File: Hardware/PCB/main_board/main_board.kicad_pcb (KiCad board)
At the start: 2 copper layers, 150 x 160 mm, 125 parts, among them J1 SWD, J2 USB_A, J3 DIN-5_180degree, J4 USB_B, J5 Conn_Coaxial, J6 AudioJack3, Q1 BC857B, Q2 BC847B, Q3 BC847B, Q4 BC857B, Q5 BC847B, U1 MCP6002-xSN, U2 NUCLEO-F446RE, U3 6N137, U4 RC4558, U5 MCP6002-xSN

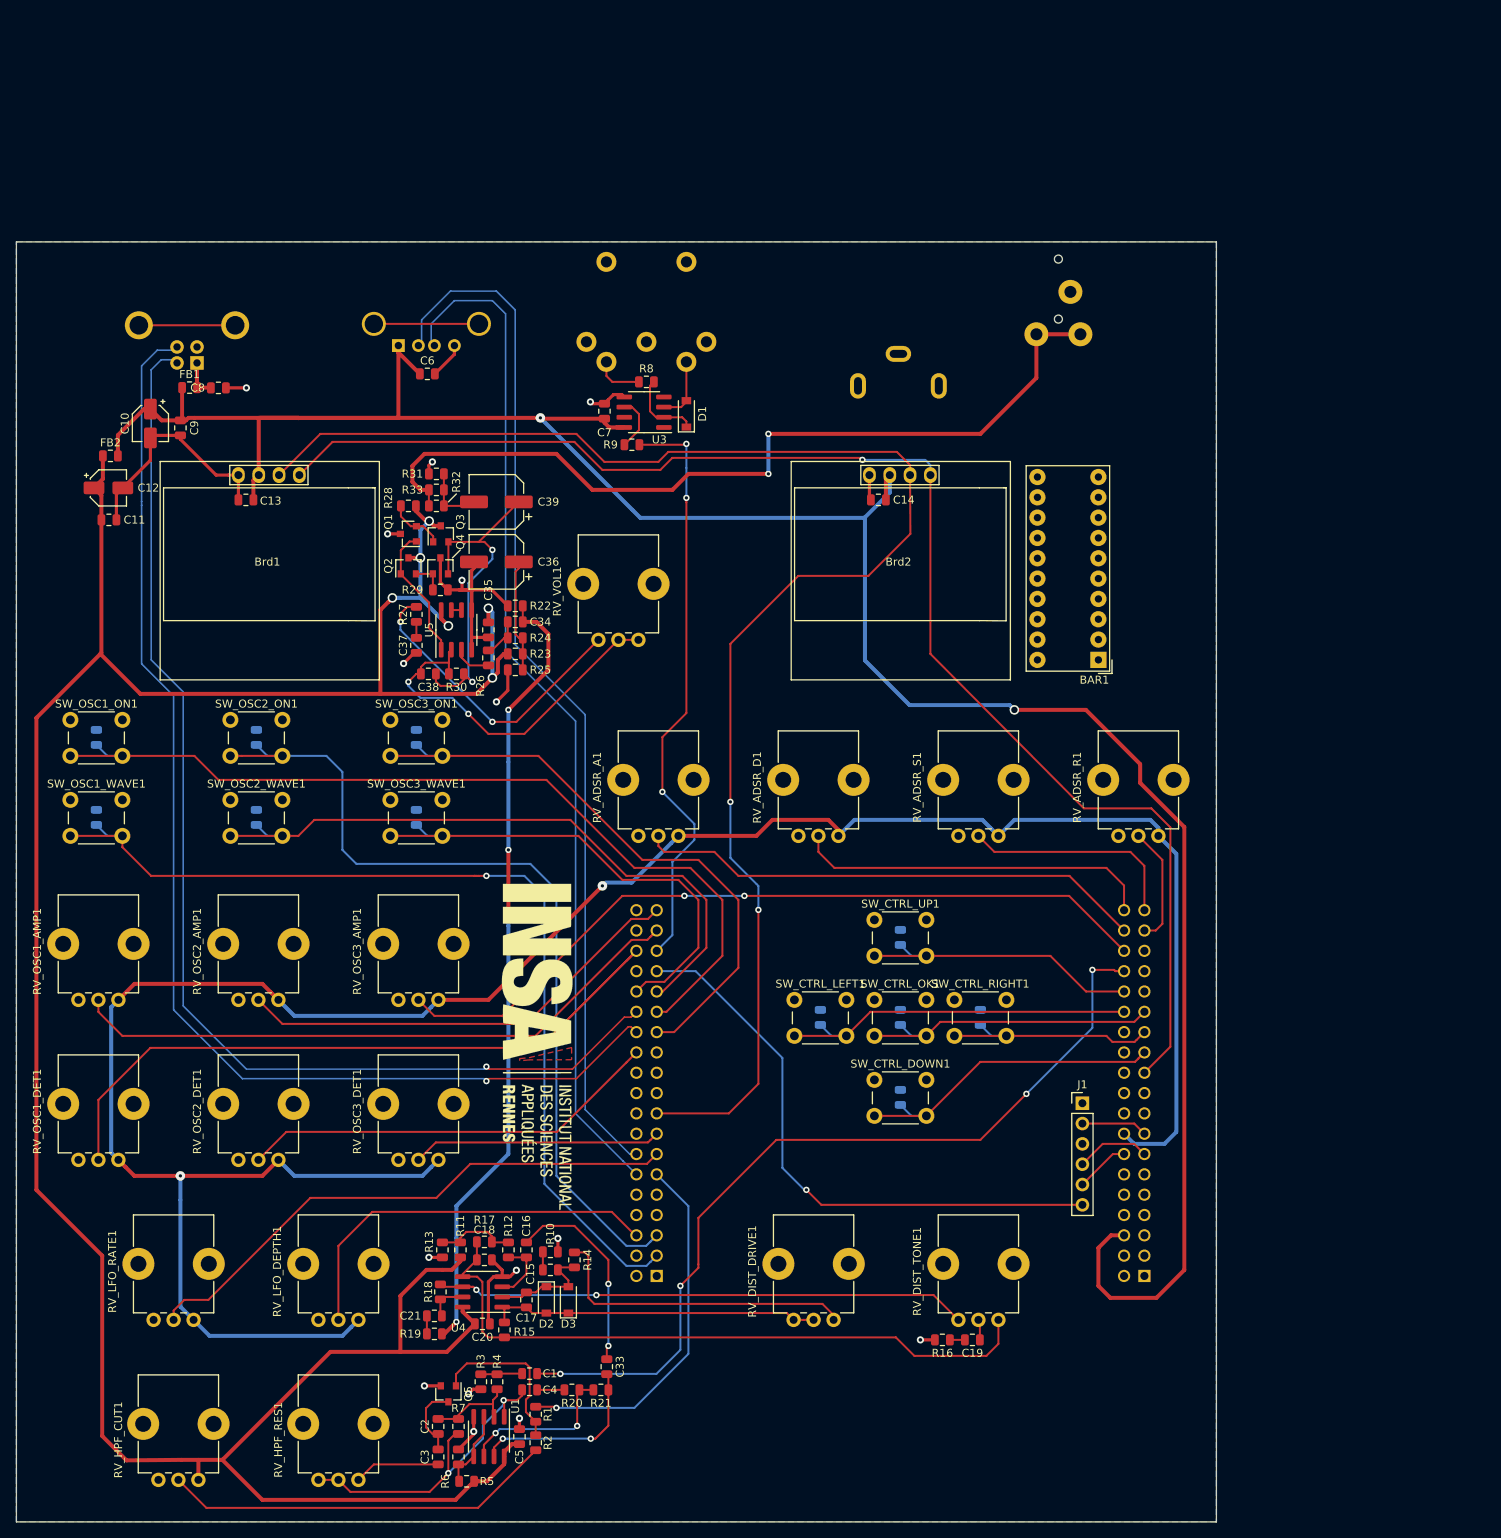
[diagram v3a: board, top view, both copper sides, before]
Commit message: Add test points headers
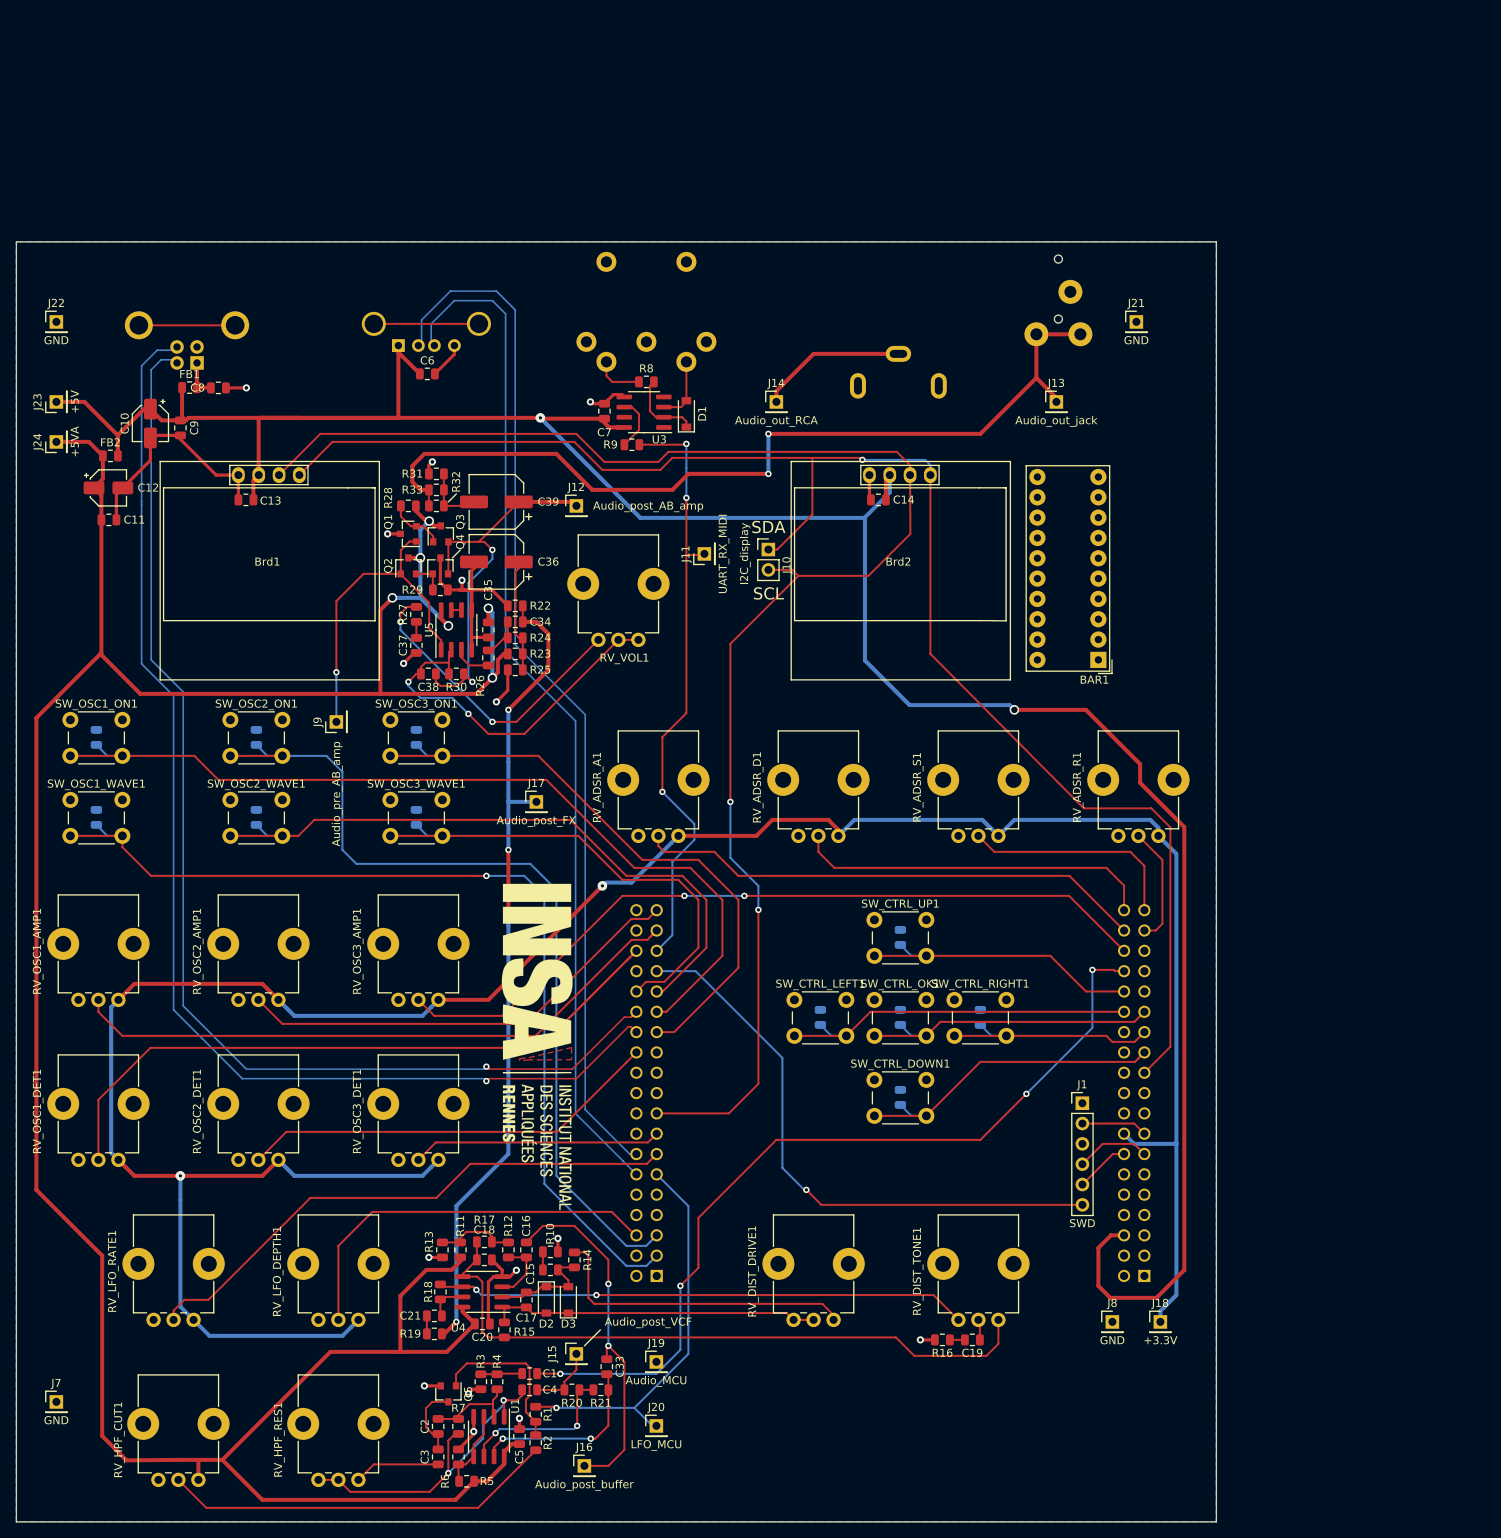
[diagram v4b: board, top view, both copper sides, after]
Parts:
- added J10: I2C_display, Connector_PinHeader_2.54mm:PinHeader_1x02_P2.54mm_Vertical, F.Cu at (129.0, 98.5)
- added J11: UART_RX_MIDI, Connector_PinHeader_2.54mm:PinHeader_1x01_P2.54mm_Vertical, F.Cu at (121.0, 99.0)
- added J12: Audio_post_AB_amp, Connector_PinHeader_2.54mm:PinHeader_1x01_P2.54mm_Vertical, F.Cu at (105.0, 93.0)
- added J13: Audio_out_jack, Connector_PinHeader_2.54mm:PinHeader_1x01_P2.54mm_Vertical, F.Cu at (165.0, 80.0)
- added J14: Audio_out_RCA, Connector_PinHeader_2.54mm:PinHeader_1x01_P2.54mm_Vertical, F.Cu at (130.0, 80.0)
- added J15: Audio_post_VCF, Connector_PinHeader_2.54mm:PinHeader_1x01_P2.54mm_Vertical, F.Cu at (105.0, 199.0)
- added J16: Audio_post_buffer, Connector_PinHeader_2.54mm:PinHeader_1x01_P2.54mm_Vertical, F.Cu at (106.0, 213.0)
- added J17: Audio_post_FX, Connector_PinHeader_2.54mm:PinHeader_1x01_P2.54mm_Vertical, F.Cu at (100.0, 130.0)
- added J18: +3.3V, Connector_PinHeader_2.54mm:PinHeader_1x01_P2.54mm_Vertical, F.Cu at (178.0, 195.0)
- added J19: Audio_MCU, Connector_PinHeader_2.54mm:PinHeader_1x01_P2.54mm_Vertical, F.Cu at (115.0, 200.0)
- added J20: LFO_MCU, Connector_PinHeader_2.54mm:PinHeader_1x01_P2.54mm_Vertical, F.Cu at (115.0, 208.0)
- added J21: GND, Connector_PinHeader_2.54mm:PinHeader_1x01_P2.54mm_Vertical, F.Cu at (175.0, 70.0)
- added J22: GND, Connector_PinHeader_2.54mm:PinHeader_1x01_P2.54mm_Vertical, F.Cu at (40.0, 70.0)
- added J23: +5V, Connector_PinHeader_2.54mm:PinHeader_1x01_P2.54mm_Vertical, F.Cu at (40.0, 80.0)
- added J24: +5VA, Connector_PinHeader_2.54mm:PinHeader_1x01_P2.54mm_Vertical, F.Cu at (40.0, 85.0)
- added J7: GND, Connector_PinHeader_2.54mm:PinHeader_1x01_P2.54mm_Vertical, F.Cu at (40.0, 205.0)
- added J8: GND, Connector_PinHeader_2.54mm:PinHeader_1x01_P2.54mm_Vertical, F.Cu at (172.0, 195.0)
- added J9: Audio_pre_AB_amp, Connector_PinHeader_2.54mm:PinHeader_1x01_P2.54mm_Vertical, F.Cu at (75.0, 120.0)
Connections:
- net Net-(C38-Pad1) renamed /audio_out/audio_post_AB_amp
- net Net-(J6-PadR) renamed /audio_out/Audio_out_jack
- net Net-(Q1-Pad1) renamed /audio_out/audio_pre_AB_amp
- J5 pad 1: Net-(J5-Pad1) -> /audio_out/Audio_out_RCA
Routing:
- net /audio_out/audio_pre_AB_amp: track 16.9 -> 41.5 mm, vias 0 -> 1
- net +3V3: track 298.4 -> 322.5 mm
- net /analogFX/IN_DIST: track 25.4 -> 45.0 mm
- net /audio_out/Audio_out_RCA: track 0.00 -> 18.5 mm
- net /HMI/I2C_display_SDA: track 177.7 -> 192.1 mm
- net +5V: track 319.7 -> 329.1 mm
- net /audio_out/audio_post_AB_amp: track 42.1 -> 49.5 mm
- net +5VA: track 356.7 -> 363.2 mm
- net /analogFX/OUT_VCF: track 3.41 -> 8.53 mm
- net /HMI/I2C_display_SCL: track 191.1 -> 195.2 mm
- net /audio_out/Audio_out_jack: track 106.6 -> 110.7 mm
- net /analogFX/CV_IN: track 46.0 -> 49.7 mm
- net /audio_out/AUDIO_IN: track 99.0 -> 102.5 mm
- net /MIDI/MIDI_Serial_RX: track 74.1 -> 76.5 mm
- net /analogFX/AUDIO_IN: track 107.0 -> 108.1 mm
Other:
- board text added: "SCL"
- board text added: "SDA"

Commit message: Re-layout HMI, pre route
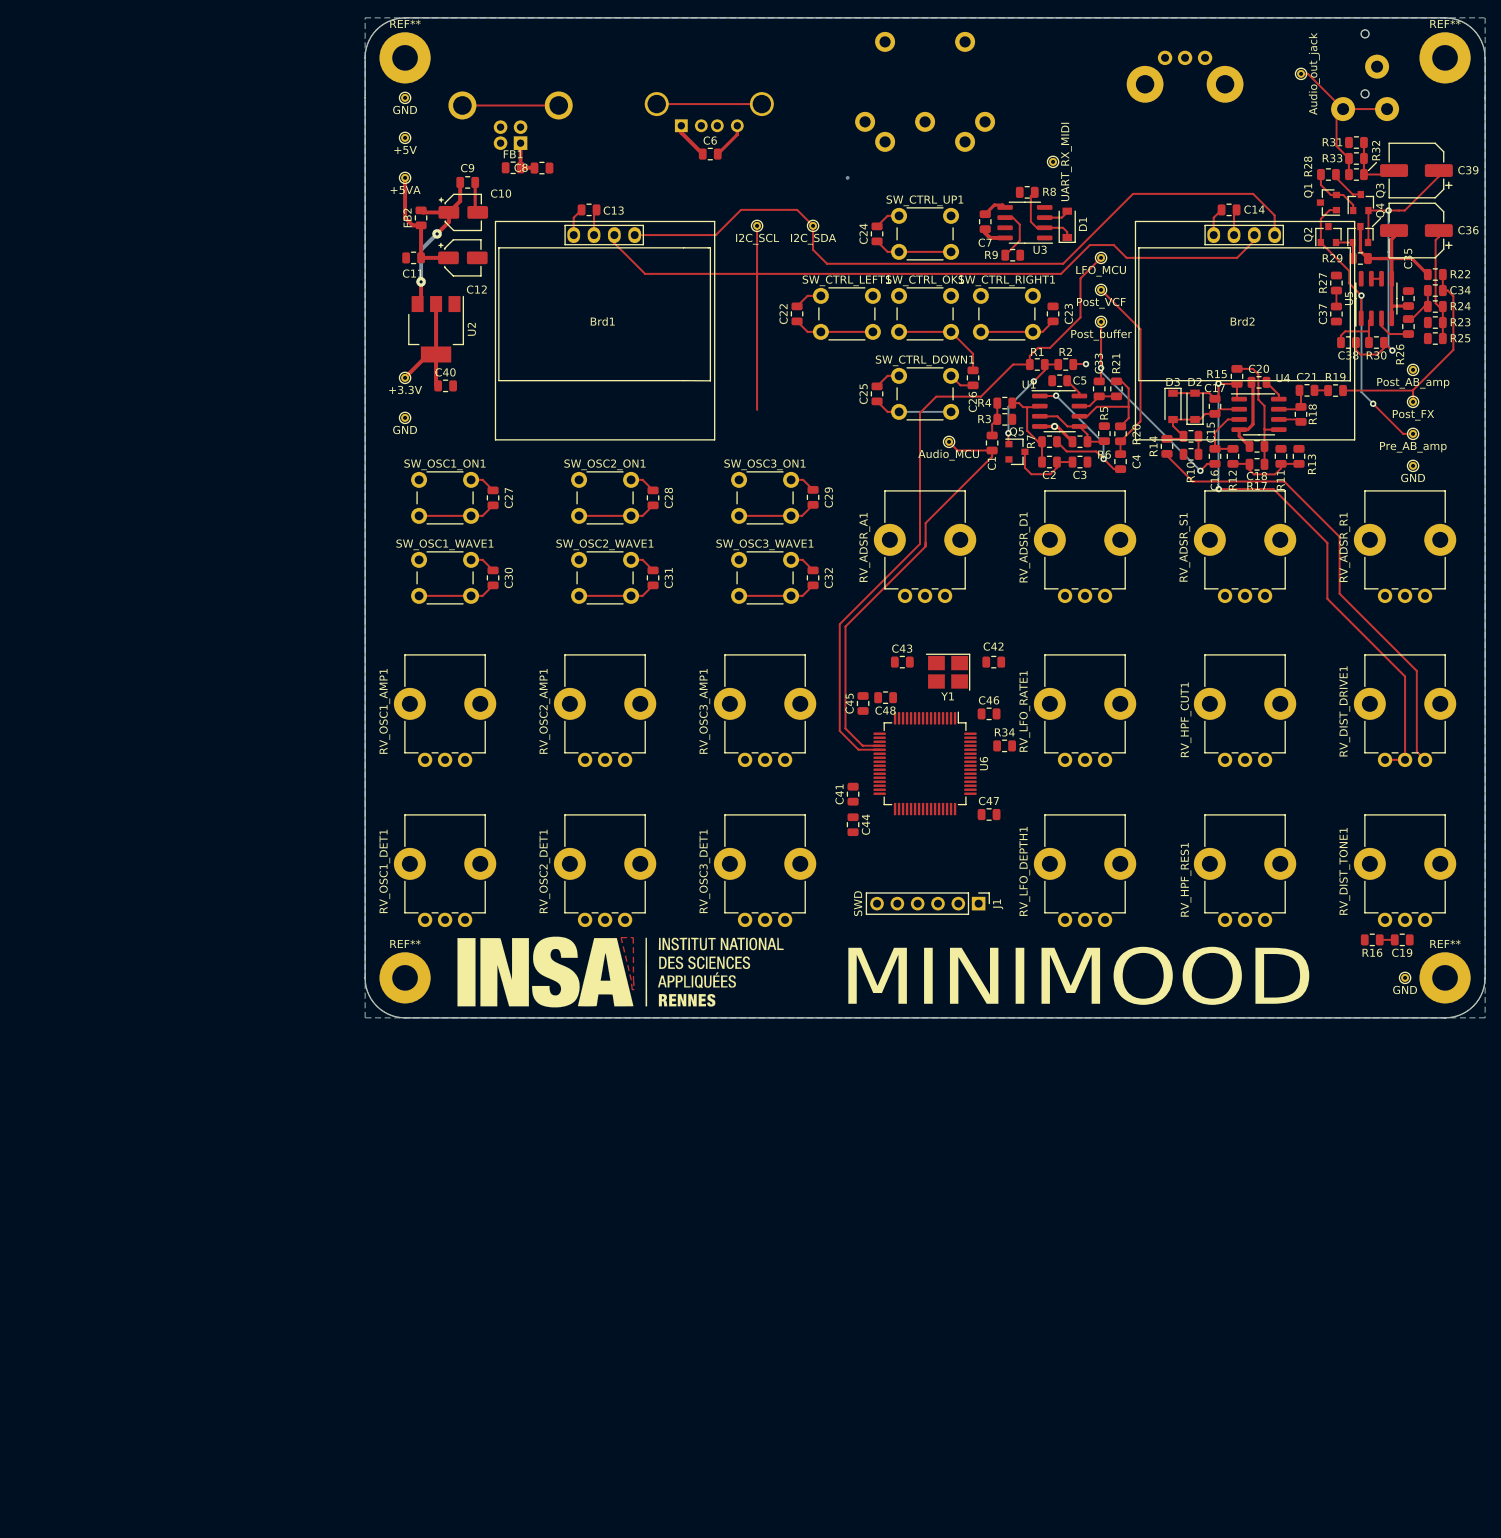
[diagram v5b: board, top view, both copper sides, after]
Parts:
- removed BAR1: HDSP-4840_2, Display:HDSP-4840
- removed J18: +3.3V, Connector_PinHeader_2.54mm:PinHeader_1x01_P2.54mm_Vertical
- added C40: 100n, Capacitor_SMD:C_0805_2012Metric, F.Cu at (88.6, 78.0)
- added C41: 4.7uF (ESR<1ohm), Capacitor_SMD:C_0805_2012Metric, F.Cu at (139.6, 129.0)
- added C42: 20p, Capacitor_SMD:C_0805_2012Metric, F.Cu at (157.2, 112.5)
- added C43: 20p, Capacitor_SMD:C_0805_2012Metric, F.Cu at (145.7, 112.5)
- added C44: 100n, Capacitor_SMD:C_0805_2012Metric, F.Cu at (139.6, 132.8)
- added C45: 100n, Capacitor_SMD:C_0805_2012Metric, F.Cu at (140.8, 117.7)
- added C46: 100n, Capacitor_SMD:C_0805_2012Metric, F.Cu at (156.6, 119.0)
- added C47: 100n, Capacitor_SMD:C_0805_2012Metric, F.Cu at (156.6, 131.6)
- added C48: 100n, Capacitor_SMD:C_0805_2012Metric, F.Cu at (143.6, 117.0)
- added R34: 10k, Resistor_SMD:R_0805_2012Metric, F.Cu at (158.5, 123.0)
- added REF**: MountingHole_3.2mm_M3_Pad, MountingHole:MountingHole_3.2mm_M3_Pad, F.Cu at (83.6, 152.0)
- added REF**: MountingHole_3.2mm_M3_Pad, MountingHole:MountingHole_3.2mm_M3_Pad, F.Cu at (213.6, 152.0)
- added REF**: MountingHole_3.2mm_M3_Pad, MountingHole:MountingHole_3.2mm_M3_Pad, F.Cu at (83.6, 37.0)
- added REF**: MountingHole_3.2mm_M3_Pad, MountingHole:MountingHole_3.2mm_M3_Pad, F.Cu at (213.6, 37.0)
- added U6: STM32F446RETx, Package_QFP:LQFP-64_10x10mm_P0.5mm, F.Cu at (148.6, 125.2)
- added Y1: Crystal, Crystal:Crystal_SMD_3225-4Pin_3.2x2.5mm_HandSoldering, F.Cu at (151.5, 113.8)
- C22, C23, C24, C25, C26, C27, C28, C29, C30, C31, C32: moved to F.Cu
- J10: value I2C_display -> I2C_SDA; footprint Connector_PinHeader_2.54mm:PinHeader_1x02_P2.54mm_Vertical -> TestPoint:TestPoint_THTPad_D1.0mm_Drill0.5mm
- J11, J13, J19, J20, J21, J22, J24, J7, J8: footprint Connector_PinHeader_2.54mm:PinHeader_1x01_P2.54mm_Vertical -> TestPoint:TestPoint_THTPad_D1.0mm_Drill0.5mm
- J12: value Audio_post_AB_amp -> Post_AB_amp; footprint Connector_PinHeader_2.54mm:PinHeader_1x01_P2.54mm_Vertical -> TestPoint:TestPoint_THTPad_D1.0mm_Drill0.5mm
- J14: value Audio_out_RCA -> +5V; footprint Connector_PinHeader_2.54mm:PinHeader_1x01_P2.54mm_Vertical -> TestPoint:TestPoint_THTPad_D1.0mm_Drill0.5mm
- J15: value Audio_post_VCF -> Post_VCF; footprint Connector_PinHeader_2.54mm:PinHeader_1x01_P2.54mm_Vertical -> TestPoint:TestPoint_THTPad_D1.0mm_Drill0.5mm
- J16: value Audio_post_buffer -> Post_buffer; footprint Connector_PinHeader_2.54mm:PinHeader_1x01_P2.54mm_Vertical -> TestPoint:TestPoint_THTPad_D1.0mm_Drill0.5mm
- J17: value Audio_post_FX -> Post_FX; footprint Connector_PinHeader_2.54mm:PinHeader_1x01_P2.54mm_Vertical -> TestPoint:TestPoint_THTPad_D1.0mm_Drill0.5mm
- J23: value +5V -> +3.3V; footprint Connector_PinHeader_2.54mm:PinHeader_1x01_P2.54mm_Vertical -> TestPoint:TestPoint_THTPad_D1.0mm_Drill0.5mm
- J5: value Conn_Coaxial -> I2C_SCL; footprint lib:rca_black -> TestPoint:TestPoint_THTPad_D1.0mm_Drill0.5mm; moved to F.Cu
- J9: value Audio_pre_AB_amp -> Pre_AB_amp; footprint Connector_PinHeader_2.54mm:PinHeader_1x01_P2.54mm_Vertical -> TestPoint:TestPoint_THTPad_D1.0mm_Drill0.5mm
- RV_VOL1: footprint Potentiometer_THT:Potentiometer_Alps_RK09K_Single_Vertical -> Potentiometer_THT:Potentiometer_Alps_RK09K_Single_Horizontal; moved to B.Cu
- U2: value NUCLEO-F446RE -> LD1117S33TR_SOT223; footprint lib:MODULE_NUCLEO-F446RE -> Package_TO_SOT_SMD:SOT-223-3_TabPin2
- moved J7 176.7 mm to (208.6, 152.0)
- moved J8 176.7 mm to (83.6, 42.0)
- moved R19 163.1 mm to (199.9, 78.6)
- moved RV_HPF_CUT1 160.9 mm to (191.1, 124.8)
- moved C21 159.0 mm to (196.3, 78.6), turned to 180 degrees
- moved J16 156.9 mm to (170.6, 70.0)
- moved J20 156.2 mm to (170.6, 62.0)
- moved R18 153.6 mm to (195.6, 81.6), turned to 90 degrees
- moved R5 153.3 mm to (171.0, 84.0), turned to 90 degrees
- moved C20 152.6 mm to (190.3, 77.6), turned to 0 degrees
- moved R15 150.3 mm to (187.6, 76.8), turned to 90 degrees
- moved R2 150.2 mm to (166.2, 75.3), turned to 0 degrees
- moved R6 148.8 mm to (167.9, 85.0), turned to 180 degrees
- moved J15 148.3 mm to (170.6, 66.0)
- moved C5 148.3 mm to (165.4, 77.4), turned to 0 degrees
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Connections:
- J14 pad 1: /audio_out/Audio_out_RCA -> +5V
- J23 pad 1: +5V -> +3V3
- J5 pad 1: /audio_out/Audio_out_RCA -> /HMI/I2C_display_SCL
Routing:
- net +5VA: track 363.2 -> 24.5 mm, vias 6 -> 0
- net +3V3: track 322.5 -> 15.2 mm, vias 2 -> 0
- net +5V: track 329.1 -> 35.4 mm
- net /power/USB_B_D+: track 152.2 -> 0.00 mm, vias 1 -> 0
- net /power/USB_B_D-: track 148.2 -> 0.00 mm, vias 1 -> 0
- net /MIDI/MIDI_USB_D-: track 129.8 -> 0.57 mm
- net /MIDI/MIDI_USB_D+: track 128.4 -> 0.57 mm
- net /MCU/GPIO_PB8: track 122.1 -> 9.79 mm, vias 1 -> 0
- net /MCU/GPIO_PB4: track 110.9 -> 9.79 mm
- net /MCU/GPIO_PB9: track 109.7 -> 9.79 mm, vias 1 -> 0
- net /HMI/I2C_display_SDA: track 192.1 -> 93.0 mm, vias 1 -> 0
- net /MCU/ADC1_IN8: track 98.1 -> 0.00 mm, vias 2 -> 0
- net /MCU/ADC1_IN14: track 96.4 -> 0.00 mm
- net /audio_out/Audio_out_jack: track 110.7 -> 21.7 mm, vias 2 -> 0
- net /HMI/I2C_display_SCL: track 195.2 -> 109.3 mm, vias 2 -> 0
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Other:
- board size 150 x 160 mm -> 140 x 125 mm
- copper layers 2 -> 4
- net class Default: clearance 0.2 -> 0.127; trace_width 0.25 -> 0.127; via_dia 0.8 -> 0.6; via_drill 0.4 -> 0.3
- net class GND removed
- net class Power removed
- rule pad_to_mask_clearance: 0.051 -> 0
- rule solder_mask_min_width: 0.25 -> 0.12
- rule trace_clearance: 0.2 -> 0.127
- rule trace_min: 0.2 -> 0.127
- rule via_min_size: 0.45 -> 0.6
- board text added: "MINIMOOD"
- board text removed: "SCL"
- board text removed: "SDA"
